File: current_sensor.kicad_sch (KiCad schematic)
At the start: 5 parts, among them J4 CSENSE

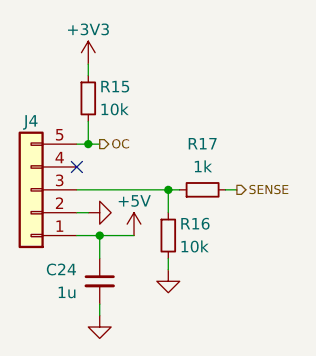
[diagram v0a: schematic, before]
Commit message: *: Switch to Molex Micro-Fit+ for main connectors
* Switch to Micro-Fit+ for power, CAN, I2C and shutdown
* Change the I2C connector pin order
* Switch to smaller Schottky diodes
* Resize the board to 85 mm x 65 mm
* Remove the charge enable output as it's currently not needed
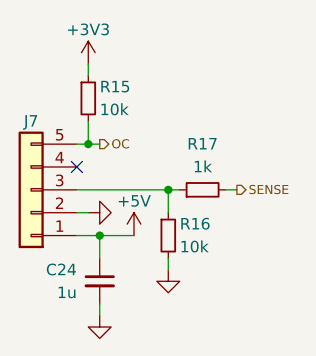
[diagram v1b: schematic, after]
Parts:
- J7: renamed from J4; value CSENSE -> Conn_01x05
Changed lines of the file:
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@@
 		(on_board yes)
 		(dnp no)
-		(property "Reference" "J4"
+		(property "Reference" "J7"
 			(at 128.27 82.55 0)
 			(effects
@@
 			)
 		)
-		(property "Value" "CSENSE"
+		(property "Value" "Conn_01x05"
 			(at 125.73 88.9001 0)
 			(effects
@@
 			(project "bms_master"
 				(path "/ff788b45-a486-492a-a3f3-4e15ca08a026/2f523f65-cf81-412e-9a3a-95bf91c61e95"
-					(reference "J4")
+					(reference "J7")
 					(unit 1)
 				)
 				(path "/ff788b45-a486-492a-a3f3-4e15ca08a026/6369dd45-ebef-424f-add8-5cbda69ab87c"
-					(reference "J5")
+					(reference "J8")
 					(unit 1)
 				)

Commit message: *: Reorder reference designators
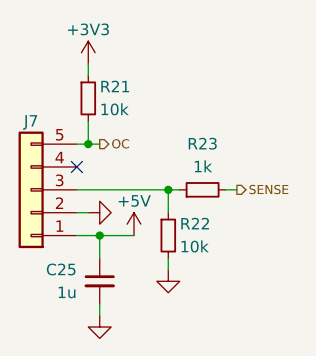
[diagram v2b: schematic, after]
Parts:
- renumbered C24 to C25, R15 to R21, R16 to R22, R17 to R23
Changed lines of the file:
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@@
 		(on_board yes)
 		(dnp no)
-		(property "Reference" "R16"
+		(property "Reference" "R22"
 			(at 144.78 93.98 0)
 			(effects
@@
 			(project "bms_master"
 				(path "/ff788b45-a486-492a-a3f3-4e15ca08a026/2f523f65-cf81-412e-9a3a-95bf91c61e95"
-					(reference "R16")
-					(unit 1)
-				)
-				(path "/ff788b45-a486-492a-a3f3-4e15ca08a026/6369dd45-ebef-424f-add8-5cbda69ab87c"
-					(reference "R19")
+					(reference "R22")
+					(unit 1)
+				)
+				(path "/ff788b45-a486-492a-a3f3-4e15ca08a026/6369dd45-ebef-424f-add8-5cbda69ab87c"
+					(reference "R25")
 					(unit 1)
 				)
@@
 		(dnp no)
 		(fields_autoplaced yes)
-		(property "Reference" "R17"
+		(property "Reference" "R23"
 			(at 147.32 85.09 90)
 			(effects
@@
 			(project "bms_master"
 				(path "/ff788b45-a486-492a-a3f3-4e15ca08a026/2f523f65-cf81-412e-9a3a-95bf91c61e95"
-					(reference "R17")
-					(unit 1)
-				)
-				(path "/ff788b45-a486-492a-a3f3-4e15ca08a026/6369dd45-ebef-424f-add8-5cbda69ab87c"
-					(reference "R20")
+					(reference "R23")
+					(unit 1)
+				)
+				(path "/ff788b45-a486-492a-a3f3-4e15ca08a026/6369dd45-ebef-424f-add8-5cbda69ab87c"
+					(reference "R26")
 					(unit 1)
 				)
@@
 		(on_board yes)
 		(dnp no)
-		(property "Reference" "R15"
+		(property "Reference" "R21"
 			(at 135.89 78.74 0)
 			(effects
@@
 			(project "bms_master"
 				(path "/ff788b45-a486-492a-a3f3-4e15ca08a026/2f523f65-cf81-412e-9a3a-95bf91c61e95"
-					(reference "R15")
-					(unit 1)
-				)
-				(path "/ff788b45-a486-492a-a3f3-4e15ca08a026/6369dd45-ebef-424f-add8-5cbda69ab87c"
-					(reference "R18")
+					(reference "R21")
+					(unit 1)
+				)
+				(path "/ff788b45-a486-492a-a3f3-4e15ca08a026/6369dd45-ebef-424f-add8-5cbda69ab87c"
+					(reference "R24")
 					(unit 1)
 				)
@@
 		(on_board yes)
 		(dnp no)
-		(property "Reference" "C24"
+		(property "Reference" "C25"
 			(at 133.35 99.0662 0)
 			(effects
@@
 			(project "bms_master"
 				(path "/ff788b45-a486-492a-a3f3-4e15ca08a026/2f523f65-cf81-412e-9a3a-95bf91c61e95"
-					(reference "C24")
-					(unit 1)
-				)
-				(path "/ff788b45-a486-492a-a3f3-4e15ca08a026/6369dd45-ebef-424f-add8-5cbda69ab87c"
 					(reference "C25")
 					(unit 1)
 				)
+				(path "/ff788b45-a486-492a-a3f3-4e15ca08a026/6369dd45-ebef-424f-add8-5cbda69ab87c"
+					(reference "C26")
+					(unit 1)
+				)

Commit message: *: Switch from the TPS25961 eFuse to the TPS26625
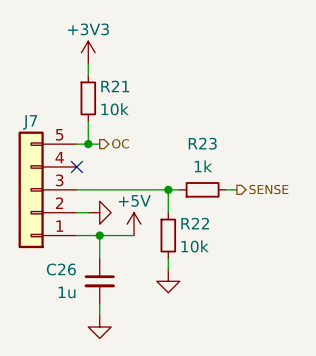
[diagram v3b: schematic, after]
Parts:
- renumbered C25 to C26
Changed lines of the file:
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@@
 		(on_board yes)
 		(dnp no)
-		(property "Reference" "C25"
+		(property "Reference" "C26"
 			(at 133.35 99.0662 0)
 			(effects
@@
 			(project "bms_master"
 				(path "/ff788b45-a486-492a-a3f3-4e15ca08a026/2f523f65-cf81-412e-9a3a-95bf91c61e95"
-					(reference "C25")
+					(reference "C26")
 					(unit 1)
 				)
 				(path "/ff788b45-a486-492a-a3f3-4e15ca08a026/6369dd45-ebef-424f-add8-5cbda69ab87c"
-					(reference "C26")
+					(reference "C27")
 					(unit 1)
 				)
